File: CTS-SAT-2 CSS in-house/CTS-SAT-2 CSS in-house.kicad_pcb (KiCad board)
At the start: 2 copper layers, 56 parts, among them J1 3v3, J2 GND, J3 SCL I2c, J4 SDA I2c, U1 POPA4383PWR, U2 POPA4383PWR, U3 ADS7128IRTET

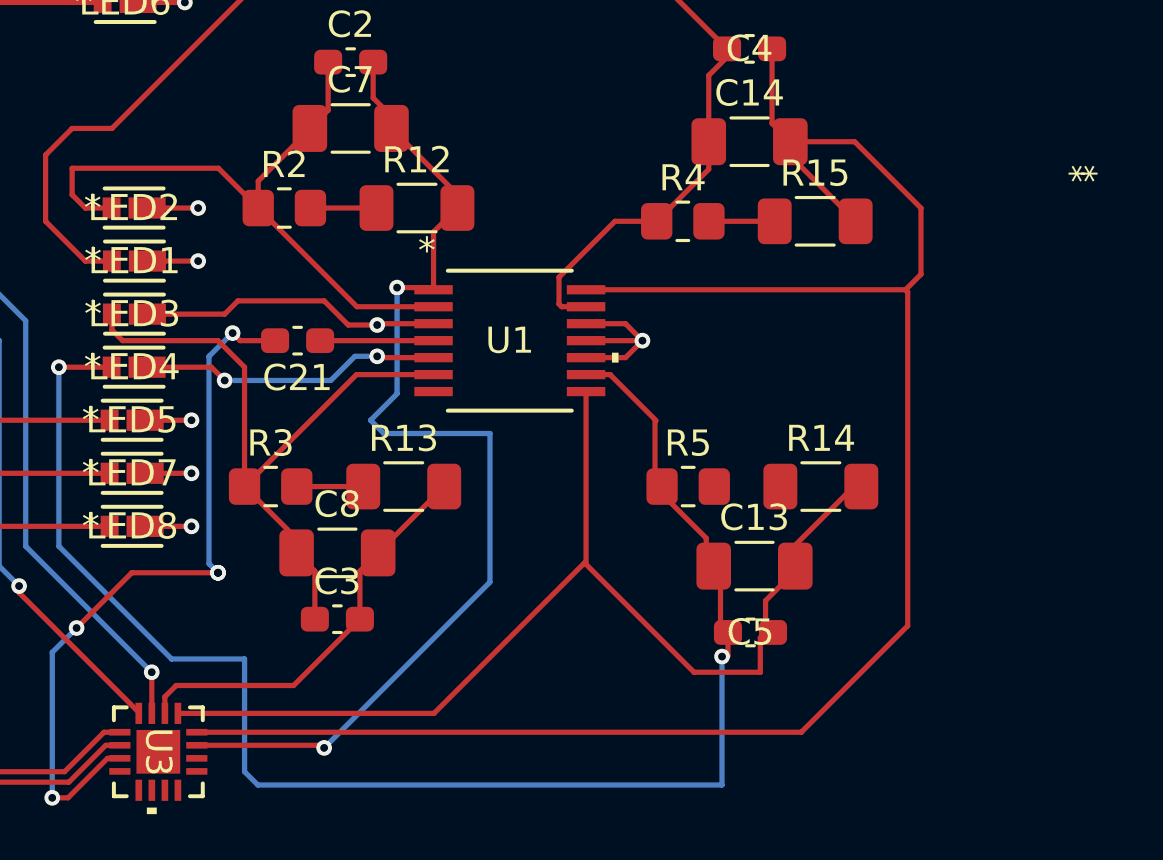
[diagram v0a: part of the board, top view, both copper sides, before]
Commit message: Update CTS-SAT-2 CSS in-house.kicad_pcb
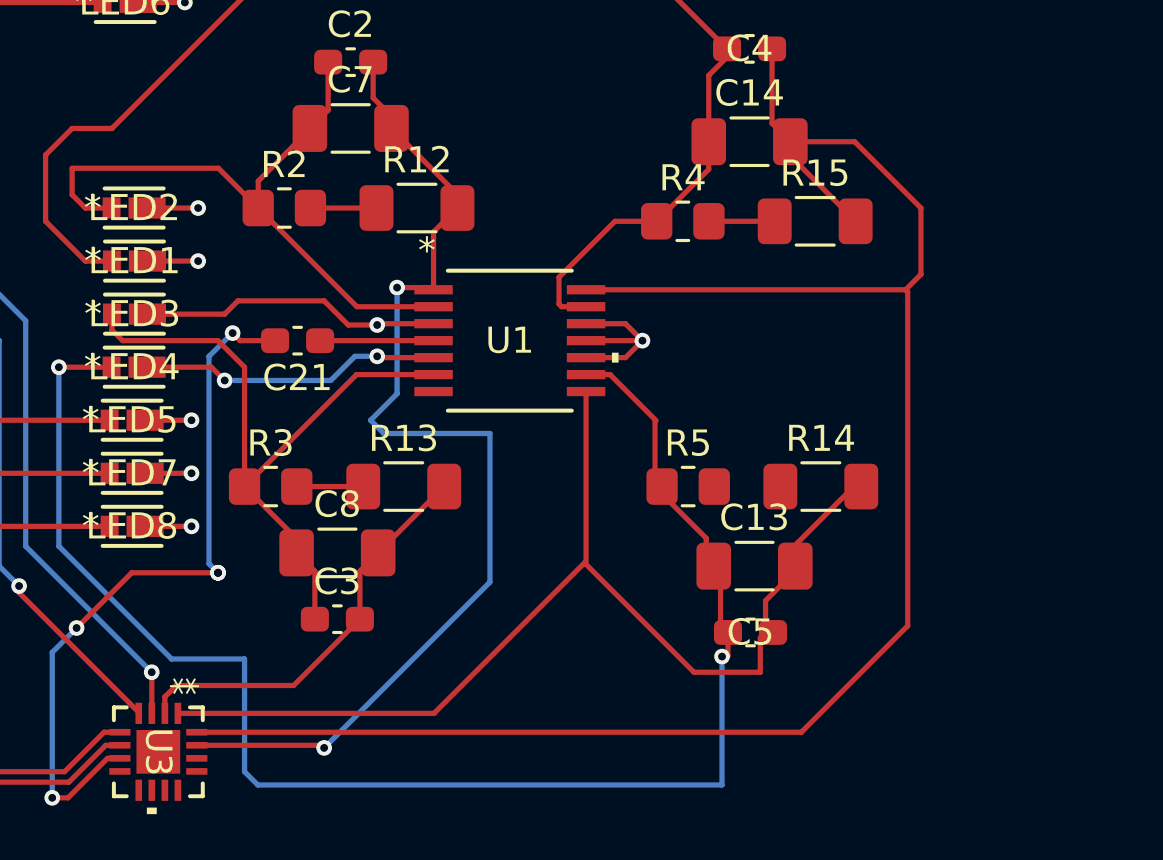
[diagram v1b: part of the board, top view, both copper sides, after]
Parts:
- LED1, LED2, LED3, LED4, LED5, LED6, LED7, LED8: footprint footprints:6p550-5363p01-4_VIS -> 6p550-5363p01-4_VIS footprints:6p550-5363p01-4_VIS
- U1, U2: footprint ul_POPA FP:TSSOP_PW_14_TEX -> ul_POPA4383PWR footprints:TSSOP_PW_14_TEX
- U3: footprint wqfm footprints:WQFN16_RTE_TEX -> WQFN16_RTE_TEX-M footprints:WQFN16_RTE_TEX
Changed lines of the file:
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@@
 		)
 	)
-	(footprint "footprints:6p550-5363p01-4_VIS"
+	(footprint "6p550-5363p01-4_VIS footprints:6p550-5363p01-4_VIS"
 		(layer "F.Cu")
 		(at 131.4196 85.344)
@@
 		)
 	)
-	(footprint "ul_POPA FP:TSSOP_PW_14_TEX"
+	(footprint "ul_POPA4383PWR footprints:TSSOP_PW_14_TEX"
 		(layer "F.Cu")
 		(at 115.57 89.154)
@@
 		)
 		(property "Value" "POPA4383PWR"
-			(at 1 0 0)
+			(at 0 0 0)
 			(unlocked yes)
 			(layer "F.Fab")
@@
 		)
 	)
-	(footprint "footprints:6p550-5363p01-4_VIS"
+	(footprint "6p550-5363p01-4_VIS footprints:6p550-5363p01-4_VIS"
 		(layer "F.Cu")
 		(at 131.3307 91.44)
@@
 		)
 	)
-	(footprint "footprints:6p550-5363p01-4_VIS"
+	(footprint "6p550-5363p01-4_VIS footprints:6p550-5363p01-4_VIS"
 		(layer "F.Cu")
 		(at 131.064 75.438)
@@
 		)
 	)
-	(footprint "ul_POPA FP:TSSOP_PW_14_TEX"
+	(footprint "ul_POPA4383PWR footprints:TSSOP_PW_14_TEX"
 		(layer "F.Cu")
 		(at 145.796 88.392)
@@
 		)
 	)
-	(footprint "footprints:6p550-5363p01-4_VIS"
+	(footprint "6p550-5363p01-4_VIS footprints:6p550-5363p01-4_VIS"
 		(layer "F.Cu")
 		(at 131.4069 89.408)
@@
 		)
 	)
-	(footprint "footprints:6p550-5363p01-4_VIS"
+	(footprint "6p550-5363p01-4_VIS footprints:6p550-5363p01-4_VIS"
 		(layer "F.Cu")
 		(at 131.4196 87.376)
@@
 		)
 	)
-	(footprint "footprints:6p550-5363p01-4_VIS"
+	(footprint "6p550-5363p01-4_VIS footprints:6p550-5363p01-4_VIS"
 		(layer "F.Cu")
 		(at 131.3307 93.472)
@@
 		)
 	)
-	(footprint "footprints:6p550-5363p01-4_VIS"
+	(footprint "6p550-5363p01-4_VIS footprints:6p550-5363p01-4_VIS"
 		(layer "F.Cu")
 		(at 131.3307 95.504)
@@
 		)
 	)
-	(footprint "footprints:6p550-5363p01-4_VIS"
+	(footprint "6p550-5363p01-4_VIS footprints:6p550-5363p01-4_VIS"
 		(layer "F.Cu")
 		(at 131.4069 83.312)
@@
 		(embedded_fonts no)
 	)
-	(footprint "wqfm footprints:WQFN16_RTE_TEX"
+	(footprint "WQFN16_RTE_TEX-M footprints:WQFN16_RTE_TEX"
 		(layer "F.Cu")
 		(at 132.334 104.14 -90)
@@
 		)
 		(property "Datasheet" "https://www.ti.com/lit/gpn/ads7128"
-			(at 0 0 90)
+			(at 0 0 270)
 			(layer "F.Fab")
 			(hide yes)
@@
 		)
 		(property "Description" ""
-			(at 0 0 90)
+			(at 0 0 270)
 			(layer "F.Fab")
 			(hide yes)
@@
 		)
 		(fp_text user "*"
-			(at -22.1461 -35.418 90)
+			(at -2.5146 -1 270)
 			(layer "F.SilkS")
 			(effects
@@
 		)
 		(fp_text user "*"
-			(at -22.1461 -35.418 270)
+			(at -2.5146 -1 270)
 			(unlocked yes)
 			(layer "F.SilkS")
@@
 		)
 		(fp_text user "*"
-			(at -1.0668 -1 90)
+			(at -1.0668 -1 270)
 			(layer "F.Fab")
 			(effects

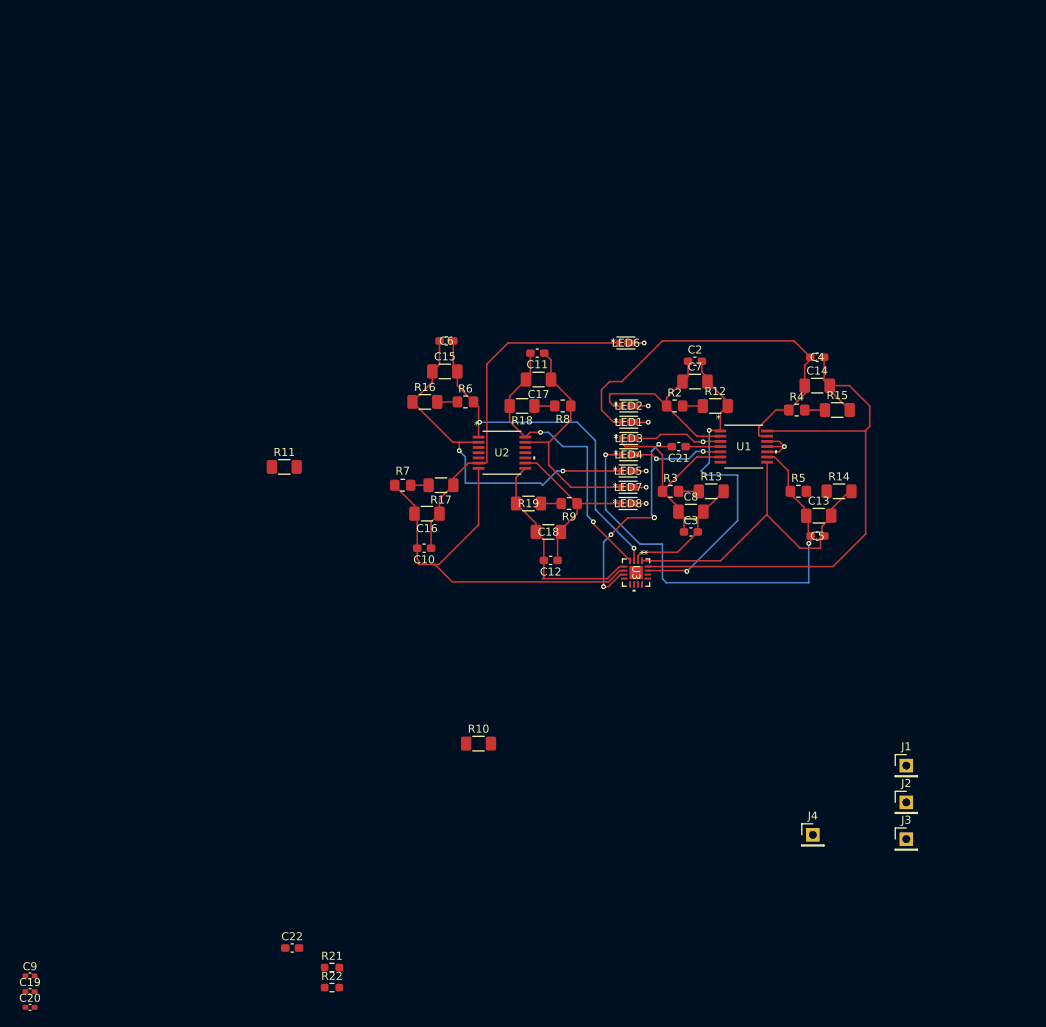
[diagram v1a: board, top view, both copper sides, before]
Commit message: Finished all comments
Completed all comments from the design review, changed DNP to sockets for testing, added virtual ground for TIAs, and other small things
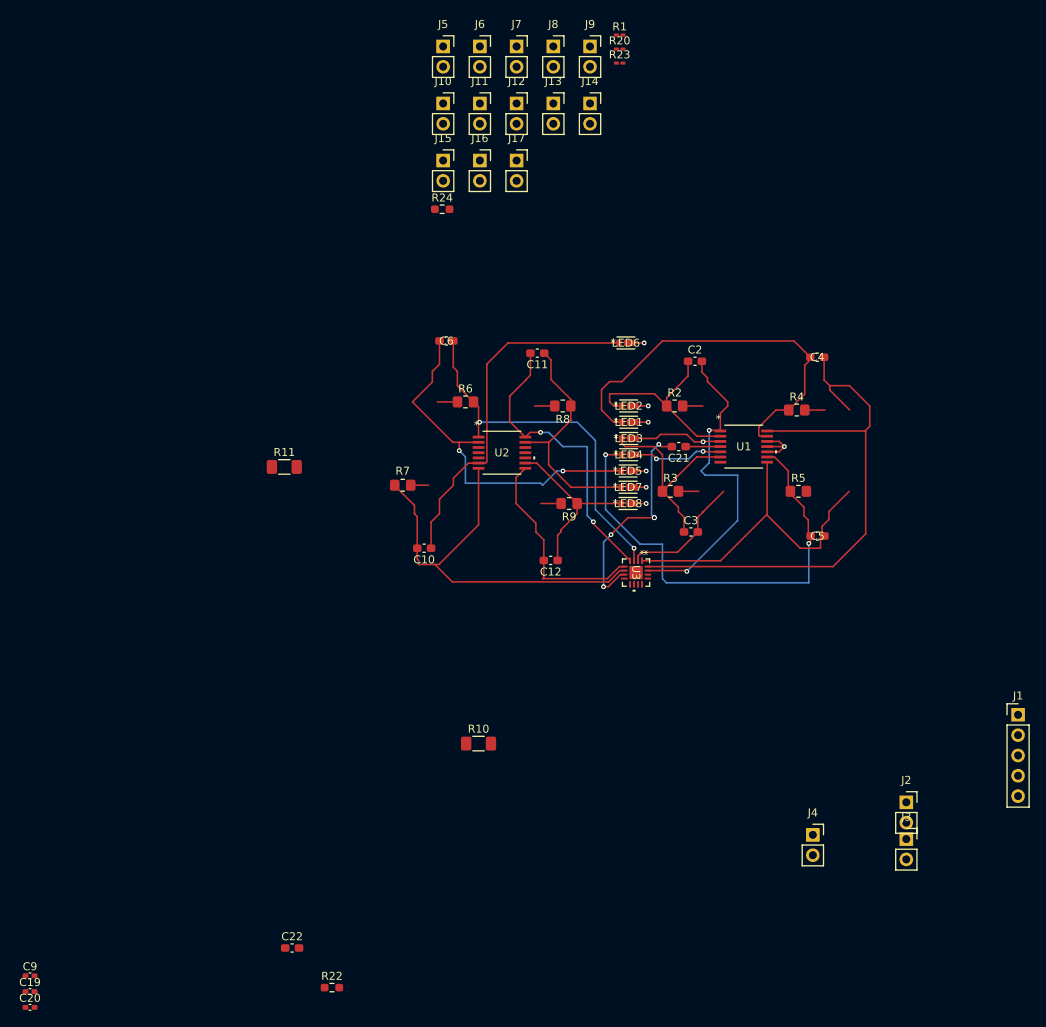
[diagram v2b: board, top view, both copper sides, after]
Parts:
- removed C13, C14, C15, C16, C17, C18, C7, C8: C, Capacitor_SMD:C_1206_3216Metric_Pad1.33x1.80mm_HandSolder
- removed R12, R13, R14, R15, R16, R17, R18, R19: R, Resistor_SMD:R_1206_3216Metric_Pad1.30x1.75mm_HandSolder
- removed R21: 4.7 kΩ, Resistor_SMD:R_0603_1608Metric_Pad0.98x0.95mm_HandSolder
- added J10: Socket_1x2, Connector_PinSocket_2.54mm:PinSocket_1x02_P2.54mm_Vertical, F.Cu at (108.2, 45.5)
- added J11: Socket_1x2, Connector_PinSocket_2.54mm:PinSocket_1x02_P2.54mm_Vertical, F.Cu at (112.8, 45.5)
- added J12: Socket_1x2, Connector_PinSocket_2.54mm:PinSocket_1x02_P2.54mm_Vertical, F.Cu at (117.4, 45.5)
- added J13: Socket_1x2, Connector_PinSocket_2.54mm:PinSocket_1x02_P2.54mm_Vertical, F.Cu at (122.0, 45.5)
- added J14: Socket_1x2, Connector_PinSocket_2.54mm:PinSocket_1x02_P2.54mm_Vertical, F.Cu at (126.6, 45.5)
- added J15: Socket_1x2, Connector_PinSocket_2.54mm:PinSocket_1x02_P2.54mm_Vertical, F.Cu at (108.2, 52.6)
- added J16: Socket_1x2, Connector_PinSocket_2.54mm:PinSocket_1x02_P2.54mm_Vertical, F.Cu at (112.8, 52.6)
- added J17: Socket_1x2, Connector_PinSocket_2.54mm:PinSocket_1x02_P2.54mm_Vertical, F.Cu at (117.4, 52.6)
- added J5: Socket_1x2, Connector_PinSocket_2.54mm:PinSocket_1x02_P2.54mm_Vertical, F.Cu at (108.2, 38.4)
- added J6: Socket_1x2, Connector_PinSocket_2.54mm:PinSocket_1x02_P2.54mm_Vertical, F.Cu at (112.8, 38.4)
- added J7: Socket_1x2, Connector_PinSocket_2.54mm:PinSocket_1x02_P2.54mm_Vertical, F.Cu at (117.4, 38.4)
- added J8: Socket_1x2, Connector_PinSocket_2.54mm:PinSocket_1x02_P2.54mm_Vertical, F.Cu at (122.0, 38.4)
- added J9: Socket_1x2, Connector_PinSocket_2.54mm:PinSocket_1x02_P2.54mm_Vertical, F.Cu at (126.6, 38.4)
- added R1: 10 kΩ, Resistor_SMD:R_0201_0603Metric_Pad0.64x0.40mm_HandSolder, F.Cu at (130.3, 37.0)
- added R20: 10 kΩ, Resistor_SMD:R_0201_0603Metric_Pad0.64x0.40mm_HandSolder, F.Cu at (130.3, 38.7)
- added R23: 10 kΩ, Resistor_SMD:R_0201_0603Metric_Pad0.64x0.40mm_HandSolder, F.Cu at (130.3, 40.5)
- added R24: 4.7 kΩ, Resistor_SMD:R_0603_1608Metric_Pad0.98x0.95mm_HandSolder, F.Cu at (108.1, 58.7)
- J1: value 3v3 -> Conn_01x05_Socket; footprint Connector_PinHeader_2.54mm:PinHeader_1x01_P2.54mm_Vertical -> Connector_PinHeader_2.54mm:PinHeader_1x05_P2.54mm_Vertical
- J2: value GND -> Socket_1x2; footprint Connector_PinHeader_2.54mm:PinHeader_1x01_P2.54mm_Vertical -> Connector_PinSocket_2.54mm:PinSocket_1x02_P2.54mm_Vertical
- J3: value SCL I2c -> Socket_1x2; footprint Connector_PinHeader_2.54mm:PinHeader_1x01_P2.54mm_Vertical -> Connector_PinSocket_2.54mm:PinSocket_1x02_P2.54mm_Vertical
- J4: value SDA I2c -> Socket_1x2; footprint Connector_PinHeader_2.54mm:PinHeader_1x01_P2.54mm_Vertical -> Connector_PinSocket_2.54mm:PinSocket_1x02_P2.54mm_Vertical
- moved J1 15.3 mm to (180.1, 121.9)
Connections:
- net Net-(LED2-ANODE) renamed /ARRAY_SIGNAL_1
- net Net-(LED3-ANODE) renamed /ARRAY_SIGNAL_2
- net Net-(LED4-ANODE) renamed /ARRAY_SIGNAL_3
- net Net-(LED6-ANODE) renamed /ARRAY_SIGNAL_5
- C10 pad 2: Net-(U2-OUT_B) -> /TIA_OUTPUT_5
- C11 pad 1: Net-(LED7-ANODE) -> /ARRAY_SIGNAL_6
- C11 pad 2: Net-(U2-OUT_D) -> /TIA_OUTPUT_6
- C12 pad 1: Net-(LED8-ANODE) -> /ARRAY_SIGNAL_7
- C12 pad 2: Net-(U2-OUT_C) -> /TIA_OUTPUT_7
- C19 pad 1: Net-(J1-Pin_1) -> /3V3_SUPPLY_1
- C19 pad 2: Earth -> GND
- C2 pad 2: Net-(U1-OUT_A) -> /TIA_OUPTUT_1
- C20 pad 1: Net-(J1-Pin_1) -> /3V3_SUPPLY_1
- C20 pad 2: Earth -> GND
- C21 pad 2: Net-(J1-Pin_1) -> /3V3_SUPPLY_1
- C22 pad 2: Net-(J1-Pin_1) -> /3V3_SUPPLY_1
- C3 pad 2: Net-(U1-OUT_B) -> /TIA_OUTPUT_2
- C4 pad 2: Net-(U1-OUT_D) -> /COURSE_TIA_OUTPUT
- C5 pad 2: Net-(U1-OUT_C) -> /TIA_OUTPUT_3
- C6 pad 1: Net-(LED5-ANODE) -> /ARRAY_SIGNAL_4
- C6 pad 2: Net-(U2-OUT_A) -> /TIA_OUTPUT_4
- C9 pad 1: Earth -> GND
- J2 pad 1: Earth -> /TIA_OUTPUT_4
- J4 pad 1: Net-(J4-Pin_1) -> /TIA_OUTPUT_6
- LED1 pad 2: Earth -> GND
- LED2 pad 2: Earth -> GND
- LED3 pad 2: Earth -> GND
- LED4 pad 2: Earth -> GND
- LED5 pad 1: Net-(LED5-ANODE) -> /ARRAY_SIGNAL_4
- LED5 pad 2: Earth -> GND
- LED6 pad 2: Earth -> GND
- LED7 pad 1: Net-(LED7-ANODE) -> /ARRAY_SIGNAL_7
- LED7 pad 2: Earth -> GND
- LED8 pad 1: Net-(LED8-ANODE) -> /ARRAY_SIGNAL_6
- LED8 pad 2: Earth -> GND
- R11 pad 1: Earth -> GND
- R22 pad 1: Net-(J1-Pin_1) -> /3V3_SUPPLY_1
- R22 pad 2: Net-(J3-Pin_1) -> Net-(J1-Pin_2)
- R6 pad 1: Net-(R16-Pad2) -> Net-(J3-Pin_1)
- R6 pad 2: Net-(U2-OUT_A) -> /TIA_OUTPUT_4
- R7 pad 2: Net-(U2-OUT_B) -> /TIA_OUTPUT_5
- R8 pad 1: Net-(LED7-ANODE) -> /ARRAY_SIGNAL_6
- R8 pad 2: Net-(R18-Pad1) -> Net-(J4-Pin_2)
- R9 pad 1: Net-(LED8-ANODE) -> /ARRAY_SIGNAL_7
- U1 pad 1: Net-(U1-OUT_A) -> /TIA_OUPTUT_1
- U1 pad 10: Earth -> /1.65V_VGND_1
- U1 pad 11: Earth -> GND
- U1 pad 12: Earth -> /1.65V_VGND_1
- U1 pad 14: Net-(U1-OUT_D) -> /COURSE_TIA_OUTPUT
- U1 pad 3: Earth -> /1.65V_VGND_1
- U1 pad 5: Earth -> /1.65V_VGND_1
- U1 pad 7: Net-(U1-OUT_B) -> /TIA_OUTPUT_2
- U1 pad 8: Net-(U1-OUT_C) -> /TIA_OUTPUT_3
- U2 pad 1: Net-(U2-OUT_A) -> /TIA_OUTPUT_4
- U2 pad 10: Earth -> /1.65V_VGND
- U2 pad 11: Earth -> GND
- U2 pad 12: Earth -> /1.65V_VGND
- U2 pad 13: Net-(LED7-ANODE) -> /ARRAY_SIGNAL_6
- U2 pad 14: Net-(U2-OUT_D) -> /TIA_OUTPUT_6
- U2 pad 2: Net-(LED5-ANODE) -> /ARRAY_SIGNAL_4
- U2 pad 3: Earth -> /1.65V_VGND_1
- U2 pad 5: Earth -> /1.65V_VGND_1
- U2 pad 7: Net-(U2-OUT_B) -> /TIA_OUTPUT_5
- U2 pad 8: Net-(U2-OUT_C) -> /TIA_OUTPUT_7
- U2 pad 9: Net-(LED8-ANODE) -> /ARRAY_SIGNAL_7
- U3 pad 1: Net-(U1-OUT_C) -> /TIA_OUTPUT_2
- U3 pad 10: Net-(J1-Pin_1) -> /3V3_SUPPLY_1
- U3 pad 12: unconnected-(U3-ALERT-Pad12) -> Net-(J1-Pin_3)
- U3 pad 13: Net-(J3-Pin_1) -> Net-(J1-Pin_2)
- U3 pad 14: Net-(J4-Pin_1) -> Net-(J1-Pin_1)
- U3 pad 15: Net-(U1-OUT_A) -> /COARSE_TIA_OUTPUT
- U3 pad 16: Net-(U1-OUT_D) -> /TIA_OUPTUT_1
- U3 pad 17: Earth -> GND
- U3 pad 2: Net-(U1-OUT_B) -> /TIA_OUTPUT_3
- U3 pad 3: Net-(U2-OUT_A) -> /TIA_OUTPUT_4
- U3 pad 4: Net-(U2-OUT_D) -> /TIA_OUTPUT_5
- U3 pad 5: Net-(U2-OUT_C) -> /TIA_OUTPUT_6
- U3 pad 6: Net-(U2-OUT_B) -> /TIA_OUTPUT_7
- U3 pad 7: Net-(J1-Pin_1) -> /3V3_SUPPLY_1
- U3 pad 9: Earth -> GND
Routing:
- net (no net): track 0.00 -> 268.1 mm, vias 0 -> 4
- net Net-(U1-OUT_D): track 71.4 -> 0.00 mm
- net /TIA_OUPTUT_1: track 0.00 -> 71.4 mm
- net Net-(U2-OUT_B): track 52.9 -> 0.00 mm
- net Net-(U2-OUT_A): track 45.9 -> 0.00 mm, vias 2 -> 0
- net /TIA_OUTPUT_4: track 0.00 -> 45.9 mm, vias 0 -> 2
- net Net-(LED5-ANODE): track 45.1 -> 0.00 mm, vias 2 -> 0
- net /ARRAY_SIGNAL_4: track 0.00 -> 45.1 mm, vias 0 -> 2
- net Net-(U1-OUT_A): track 41.7 -> 0.00 mm, vias 2 -> 0
- net Net-(U1-OUT_C): track 41.6 -> 0.00 mm
- net GND: track 0.00 -> 41.6 mm, vias 0 -> 10
- net Earth: track 41.6 -> 0.00 mm, vias 10 -> 0
- net Net-(U2-OUT_D): track 37.6 -> 0.00 mm, vias 2 -> 0
- net Net-(LED7-ANODE): track 29.7 -> 0.00 mm
- net Net-(J1-Pin_1): track 27.9 -> 0.00 mm, vias 5 -> 0
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
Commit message: More work on PCB routing
Rough draft
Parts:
- removed R10, R11: Adress Select, Resistor_SMD:R_1206_3216Metric_Pad1.30x1.75mm_HandSolder
- added J18: Socket_1x2, Connector_PinSocket_2.54mm:PinSocket_1x02_P2.54mm_Vertical_SMD_Pin1Left, F.Cu at (126.4, 109.5)
- added J19: Socket_1x2, Connector_PinSocket_2.54mm:PinSocket_1x02_P2.54mm_Vertical_SMD_Pin1Left, F.Cu at (133.7, 109.7)
- J10, J11, J12, J13, J14, J15, J16, J17, J2, J3, J4, J5, J6, J7, J8, J9: footprint Connector_PinSocket_2.54mm:PinSocket_1x02_P2.54mm_Vertical -> Connector_PinSocket_2.54mm:PinSocket_1x02_P2.54mm_Vertical_SMD_Pin1Left
- moved C20 85.8 mm to (133.3, 120.1), turned to 180 degrees
- moved C9 85.5 mm to (133.4, 117.1), turned to 180 degrees
- moved J3 83.6 mm to (101.7, 84.1), turned to 180 degrees
- moved J2 83.2 mm to (104.5, 77.0), turned to 180 degrees
- moved R20 81.4 mm to (123.2, 119.8), turned to -90 degrees
- moved C19 79.5 mm to (125.2, 116.4), turned to 180 degrees
- moved R23 79.4 mm to (127.0, 119.8), turned to 90 degrees
- moved J15 79.1 mm to (167.1, 105.4)
- moved J11 71.2 mm to (149.6, 106.4)
- moved R22 70.2 mm to (137.7, 100.8), turned to 90 degrees
- moved J7 67.3 mm to (116.5, 105.7)
- moved J14 66.5 mm to (170.7, 95.2)
- moved J12 64.7 mm to (170.4, 82.5), turned to 180 degrees
- moved R1 64.1 mm to (134.6, 100.9), turned to 90 degrees
- moved J4 62.1 mm to (121.4, 84.3), turned to 180 degrees
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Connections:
- U2 pad 10: /1.65V_VGND -> /1.65V_VGND_1
- U2 pad 12: /1.65V_VGND -> /1.65V_VGND_1
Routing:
- net (no net): track 268.1 -> 0.00 mm, vias 4 -> 0
- net /1.65V_VGND_1: track 0.00 -> 151.0 mm, vias 0 -> 4
- net /TIA_OUPTUT_1: track 71.4 -> 0.00 mm
- net /ARRAY_SIGNAL_3: track 59.3 -> 0.00 mm, vias 2 -> 0
- net Net-(J13-Pin_2): track 49.6 -> 0.00 mm
- net GND: track 41.6 -> 0.00 mm, vias 10 -> 0
- net /TIA_OUTPUT_5: track 0.00 -> 38.0 mm, vias 0 -> 2
- net /TIA_OUTPUT_6: track 0.00 -> 35.1 mm, vias 0 -> 2
- net /TIA_OUTPUT_7: track 0.00 -> 33.0 mm
- net /ARRAY_SIGNAL_7: track 0.00 -> 32.1 mm, vias 0 -> 2
- net /ARRAY_SIGNAL_6: track 0.00 -> 31.0 mm, vias 0 -> 2
- net Net-(J18-Pin_2): track 0.00 -> 30.6 mm
- net /3V3_SUPPLY_1: track 27.9 -> 57.4 mm, vias 5 -> 2
- net /ARRAY_SIGNAL_2: track 26.1 -> 0.00 mm
- net /ARRAY_SIGNAL_1: track 25.5 -> 0.00 mm
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
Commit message: Minor changes
Minor revisions
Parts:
- removed J10, J11, J14, J15, J16, J17, J2, J3, J4, J5, J6, J7, J8, J9: Socket_1x2, Connector_PinSocket_2.54mm:PinSocket_1x02_P2.54mm_Vertical_SMD_Pin1Left
- added C1: C, Capacitor_SMD:C_0603_1608Metric_Pad1.08x0.95mm_HandSolder, F.Cu at (102.5, 105.7)
- added C13: C, Capacitor_SMD:C_0603_1608Metric_Pad1.08x0.95mm_HandSolder, F.Cu at (118.6, 94.5)
- added C14: C, Capacitor_SMD:C_0603_1608Metric_Pad1.08x0.95mm_HandSolder, F.Cu at (156.2, 97.5)
- added C15: C, Capacitor_SMD:C_0603_1608Metric_Pad1.08x0.95mm_HandSolder, F.Cu at (155.8, 80.3)
- added C16: C, Capacitor_SMD:C_0603_1608Metric_Pad1.08x0.95mm_HandSolder, F.Cu at (176.9, 95.8)
- added C7: C, Capacitor_SMD:C_0603_1608Metric_Pad1.08x0.95mm_HandSolder, F.Cu at (107.8, 81.5)
- added C8: C, Capacitor_SMD:C_0603_1608Metric_Pad1.08x0.95mm_HandSolder, F.Cu at (114.2, 83.8)
- added R10: R, Resistor_SMD:R_0603_1608Metric_Pad0.98x0.95mm_HandSolder, F.Cu at (100.2, 100.1)
- added R11: R, Resistor_SMD:R_0603_1608Metric_Pad0.98x0.95mm_HandSolder, F.Cu at (107.8, 79.2)
- added R12: R, Resistor_SMD:R_0603_1608Metric_Pad0.98x0.95mm_HandSolder, F.Cu at (114.1, 79.2)
- added R13: R, Resistor_SMD:R_0603_1608Metric_Pad0.98x0.95mm_HandSolder, F.Cu at (114.3, 105.2)
- added R14: R, Resistor_SMD:R_0603_1608Metric_Pad0.98x0.95mm_HandSolder, F.Cu at (144.4, 95.5)
- added R15: R, Resistor_SMD:R_0603_1608Metric_Pad0.98x0.95mm_HandSolder, F.Cu at (147.2, 82.8)
- added R16: R, Resistor_SMD:R_0603_1608Metric_Pad0.98x0.95mm_HandSolder, F.Cu at (169.8, 93.0)
- moved C6 2.05 mm to (107.8, 83.8), turned to 180 degrees
- moved C11 1.80 mm to (114.2, 81.5), turned to 0 degrees
- moved R8 1.30 mm to (114.3, 86.4), turned to 180 degrees
- moved R6 0.56 mm to (107.7, 86.4)
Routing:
- net /1.65V_VGND_1: track 151.0 -> 0.00 mm, vias 4 -> 0
- net /3V3_SUPPLY_1: track 57.4 -> 0.00 mm, vias 2 -> 0
- net /TIA_OUTPUT_5: track 38.0 -> 0.00 mm, vias 2 -> 0
- net /TIA_OUTPUT_7: track 33.0 -> 0.00 mm
- net /ARRAY_SIGNAL_7: track 32.1 -> 0.00 mm, vias 2 -> 0
- net /ARRAY_SIGNAL_5: track 30.8 -> 0.00 mm
- net Net-(J18-Pin_2): track 30.6 -> 0.00 mm
- net Net-(J18-Pin_1): track 19.4 -> 0.00 mm
- net Net-(R13-Pad1): track 17.0 -> 0.00 mm, vias 2 -> 0
- net /ARRAY_SIGNAL_4: track 60.8 -> 46.8 mm
- net Net-(U2-V+): track 5.31 -> 0.00 mm
- net Net-(R10-Pad2): track 4.94 -> 0.00 mm
- net /ARRAY_SIGNAL_6: track 31.0 -> 26.4 mm, vias 2 -> 0
- net /TIA_OUTPUT_6: track 35.1 -> 38.9 mm
- net Net-(R11-Pad1): track 4.71 -> 8.14 mm, vias 2 -> 0
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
